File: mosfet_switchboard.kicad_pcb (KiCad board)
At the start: 2 copper layers, 5 parts, among them J1 Conn_01x02_Male, J2 Power Output, J3 Power Input, U1 ZXGD3006E6

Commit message: use USB-C and add analog filtering
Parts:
- removed J1: Conn_01x02_Male, Connector_PinSocket_2.54mm:PinSocket_1x02_P2.54mm_Vertical
- removed J2: Power Output, TerminalBlock_RND:TerminalBlock_RND_205-00287_1x02_P5.08mm_Horizontal
- removed J3: Power Input, TerminalBlock_RND:TerminalBlock_RND_205-00287_1x02_P5.08mm_Horizontal
- removed R1: 100Ω, Resistor_SMD:R_0402_1005Metric
- removed U1: ZXGD3006E6, Package_TO_SOT_SMD:SOT-23-6

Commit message: initial component placement
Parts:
- added C1: 220pF, Capacitor_SMD:C_0603_1608Metric, F.Cu at (146.0, 56.0)
- added C10: 100nF, Capacitor_SMD:C_0603_1608Metric, F.Cu at (138.0, 70.8)
- added C11: 10nF, Capacitor_SMD:C_0603_1608Metric, F.Cu at (145.2, 75.2)
- added C12: 100nF, Capacitor_SMD:C_0603_1608Metric, F.Cu at (137.0, 73.8)
- added C13: 1µF, Capacitor_SMD:C_0603_1608Metric, F.Cu at (147.0, 75.2)
- added C14: 4.7µF, Capacitor_SMD:C_0603_1608Metric, F.Cu at (135.0, 75.2)
- added C15: 4.7µF, Capacitor_SMD:C_0603_1608Metric, F.Cu at (138.8, 73.8)
- added C16: 4.7µF, Capacitor_SMD:C_0603_1608Metric, F.Cu at (145.2, 87.2)
- added C2: 220pF, Capacitor_SMD:C_0603_1608Metric, F.Cu at (146.0, 105.0)
- added C3: 220pF, Capacitor_SMD:C_0603_1608Metric, F.Cu at (146.2, 92.0)
- added C4: 220pF, Capacitor_SMD:C_0603_1608Metric, F.Cu at (145.0, 70.0)
- added C5: 10µF, Capacitor_SMD:C_0603_1608Metric, F.Cu at (141.0, 42.0)
- added C6: 10µF, Capacitor_SMD:C_0603_1608Metric, F.Cu at (132.0, 48.0)
- added C7: 100nF, Capacitor_SMD:C_0603_1608Metric, F.Cu at (133.2, 80.5)
- added C8: 100nF, Capacitor_SMD:C_0603_1608Metric, F.Cu at (133.2, 77.2)
- added C9: 100nF, Capacitor_SMD:C_0603_1608Metric, F.Cu at (147.0, 85.5)
- added D1: GREEN, LED_SMD:LED_0603_1608Metric, F.Cu at (161.2, 96.0)
- added D10: BZX84C3V3-T1, Diode_SMD:D_SOT-23_ANK, F.Cu at (151.0, 114.0)
- added D11: BZX84C3V3-T1, Diode_SMD:D_SOT-23_ANK, F.Cu at (151.0, 48.0)
- added D12: BZX84C3V3-T1, Diode_SMD:D_SOT-23_ANK, F.Cu at (152.0, 95.0)
- added D13: BZX84C3V3-T1, Diode_SMD:D_SOT-23_ANK, F.Cu at (151.0, 66.0)
- added D14: BZX84C3V3-T1, Diode_SMD:D_SOT-23_ANK, F.Cu at (151.0, 44.0)
- added D15: BZX84C3V3-T1, Diode_SMD:D_SOT-23_ANK, F.Cu at (152.0, 105.0)
- added D16: BZX84C3V3-T1, Diode_SMD:D_SOT-23_ANK, F.Cu at (151.0, 62.0)
- added D17: BZX84C3V3-T1, Diode_SMD:D_SOT-23_ANK, F.Cu at (152.0, 86.0)
- added D18: BLUE, LED_SMD:LED_0603_1608Metric, F.Cu at (132.0, 32.8)
- added D2: GREEN, LED_SMD:LED_0603_1608Metric, F.Cu at (161.2, 76.0)
- added D3: GREEN, LED_SMD:LED_0603_1608Metric, F.Cu at (161.0, 56.0)
- added D4: GREEN, LED_SMD:LED_0603_1608Metric, F.Cu at (161.0, 116.0)
- added D5: RED, LED_SMD:LED_0603_1608Metric, F.Cu at (157.0, 116.0)
- added D6: RED, LED_SMD:LED_0603_1608Metric, F.Cu at (157.2, 56.0)
- added D7: RED, LED_SMD:LED_0603_1608Metric, F.Cu at (157.0, 96.0)
- added D8: RED, LED_SMD:LED_0603_1608Metric, F.Cu at (157.2, 76.0)
- added D9: BZX84C3V3-T1, Diode_SMD:D_SOT-23_ANK, F.Cu at (157.0, 130.0)
- added FB1: 100Ohm @ 100MHz, Inductor_SMD:L_0805_2012Metric, F.Cu at (137.2, 40.9)
- added J1: Power Output, TerminalBlock_RND:TerminalBlock_RND_205-00287_1x02_P5.08mm_Horizontal, F.Cu at (177.0, 50.0)
- added J2: Power Output, TerminalBlock_RND:TerminalBlock_RND_205-00287_1x02_P5.08mm_Horizontal, F.Cu at (177.0, 70.0)
- added J3: Power Output, TerminalBlock_RND:TerminalBlock_RND_205-00287_1x02_P5.08mm_Horizontal, F.Cu at (177.0, 90.0)
- added J4: Power Output, TerminalBlock_RND:TerminalBlock_RND_205-00287_1x02_P5.08mm_Horizontal, F.Cu at (177.0, 110.0)
- added J5: Power Input, TerminalBlock_RND:TerminalBlock_RND_205-00287_1x02_P5.08mm_Horizontal, F.Cu at (165.0, 30.0)
- added J6: Power Input, TerminalBlock_RND:TerminalBlock_RND_205-00287_1x02_P5.08mm_Horizontal, F.Cu at (170.1, 133.0)
- added J7: USB_C_Receptacle_USB2.0, Connector_USB:USB_C_Receptacle_Amphenol_12401610E4-2A, B.Cu at (139.2, 29.0)
- added J8: Conn_01x04_Male, Connector_PinHeader_2.54mm:PinHeader_1x04_P2.54mm_Vertical, F.Cu at (153.0, 34.0)
- added J9: Conn_ARM_JTAG_SWD_10, Connector_PinHeader_1.27mm:PinHeader_2x05_P1.27mm_Vertical_SMD, F.Cu at (135.0, 106.0)
- added JP1: SolderJumper_2_Open, Jumper:SolderJumper-2_P1.3mm_Open_RoundedPad1.0x1.5mm, F.Cu at (132.5, 73.5)
- added JP3: SolderJumper_2_Open, Jumper:SolderJumper-2_P1.3mm_Open_RoundedPad1.0x1.5mm, F.Cu at (132.8, 87.2)
- added JP8: SolderJumper_3_Bridged12, Jumper:SolderJumper-3_P1.3mm_Bridged12_RoundedPad1.0x1.5mm_NumberLabels, F.Cu at (147.8, 36.8)
- added L1: 39nH, Inductor_SMD:L_0603_1608Metric, F.Cu at (143.5, 73.8)
- added R1: 12kΩ, Resistor_SMD:R_0603_1608Metric, F.Cu at (161.0, 125.0)
- added R10: 10kΩ, Resistor_SMD:R_0603_1608Metric, F.Cu at (161.2, 100.0)
- added R11: 10kΩ, Resistor_SMD:R_0603_1608Metric, F.Cu at (161.2, 80.0)
- added R12: 10kΩ, Resistor_SMD:R_0603_1608Metric, F.Cu at (161.0, 120.0)
- added R13: 10kΩ, Resistor_SMD:R_0603_1608Metric, F.Cu at (161.0, 60.0)
- added R14: 10kΩ, Resistor_SMD:R_0603_1608Metric, F.Cu at (157.0, 120.0)
- added R15: 10kΩ, Resistor_SMD:R_0603_1608Metric, F.Cu at (157.0, 80.0)
- added R16: 10kΩ, Resistor_SMD:R_0603_1608Metric, F.Cu at (157.0, 100.0)
- added R17: 10kΩ, Resistor_SMD:R_0603_1608Metric, F.Cu at (157.0, 60.0)
- added R18: 4.7kΩ, Resistor_SMD:R_0603_1608Metric, F.Cu at (155.0, 71.0)
- added R19: 4.7kΩ, Resistor_SMD:R_0603_1608Metric, F.Cu at (156.0, 89.0)
- added R2: 1.8kΩ, Resistor_SMD:R_0603_1608Metric, F.Cu at (157.0, 125.0)
- added R20: 4.7kΩ, Resistor_SMD:R_0603_1608Metric, F.Cu at (155.0, 51.0)
- added R21: 4.7kΩ, Resistor_SMD:R_0603_1608Metric, F.Cu at (155.0, 109.0)
- added R22: 4.7kΩ, Resistor_SMD:R_0603_1608Metric, F.Cu at (151.0, 111.0)
- added R23: 4.7kΩ, Resistor_SMD:R_0603_1608Metric, F.Cu at (151.8, 91.0)
- added R24: 4.7kΩ, Resistor_SMD:R_0603_1608Metric, F.Cu at (150.8, 69.0)
- added R25: 4.7kΩ, Resistor_SMD:R_0603_1608Metric, F.Cu at (151.0, 51.0)
- added R26: 4.7kΩ, Resistor_SMD:R_0603_1608Metric, F.Cu at (159.0, 113.0)
- added R27: 4.7kΩ, Resistor_SMD:R_0603_1608Metric, F.Cu at (159.0, 93.0)
- added R28: 4.7kΩ, Resistor_SMD:R_0603_1608Metric, F.Cu at (159.0, 73.0)
- added R29: 4.7kΩ, Resistor_SMD:R_0603_1608Metric, F.Cu at (159.0, 53.0)
- added R3: 5.1kΩ 1%, Resistor_SMD:R_0603_1608Metric, F.Cu at (138.2, 37.0)
- added R30: 8.2kΩ, Resistor_SMD:R_0603_1608Metric, F.Cu at (159.0, 88.8)
- added R31: 8.2kΩ, Resistor_SMD:R_0603_1608Metric, F.Cu at (159.0, 69.0)
- added R32: 8.2kΩ, Resistor_SMD:R_0603_1608Metric, F.Cu at (159.0, 109.0)
- added R33: 8.2kΩ, Resistor_SMD:R_0603_1608Metric, F.Cu at (159.0, 49.0)
- added R34: 1.8kΩ, Resistor_SMD:R_0603_1608Metric, F.Cu at (157.0, 85.0)
- added R35: 1.8kΩ, Resistor_SMD:R_0603_1608Metric, F.Cu at (157.2, 45.0)
- added R36: 1.8kΩ, Resistor_SMD:R_0603_1608Metric, F.Cu at (157.0, 65.0)
- added R37: 1.8kΩ, Resistor_SMD:R_0603_1608Metric, F.Cu at (157.0, 105.0)
- added R38: 10kΩ, Resistor_SMD:R_0603_1608Metric, F.Cu at (133.2, 83.8)
- added R39: 12kΩ, Resistor_SMD:R_0603_1608Metric, F.Cu at (161.2, 45.0)
- added R4: 10kΩ, Resistor_SMD:R_0603_1608Metric, F.Cu at (132.8, 70.5)
- added R40: 12kΩ, Resistor_SMD:R_0603_1608Metric, F.Cu at (161.0, 65.0)
- added R41: 12kΩ, Resistor_SMD:R_0603_1608Metric, F.Cu at (161.0, 105.0)
- added R42: 12kΩ, Resistor_SMD:R_0603_1608Metric, F.Cu at (161.0, 85.0)
- added R43: 10kΩ, Resistor_SMD:R_0603_1608Metric, F.Cu at (132.0, 37.0)
- added R5: 4.7kΩ, Resistor_SMD:R_0603_1608Metric, F.Cu at (146.0, 54.0)
- added R6: 4.7kΩ, Resistor_SMD:R_0603_1608Metric, F.Cu at (146.0, 107.0)
- added R7: 4.7kΩ, Resistor_SMD:R_0603_1608Metric, F.Cu at (145.0, 68.0)
- added R8: 4.7kΩ, Resistor_SMD:R_0603_1608Metric, F.Cu at (146.2, 94.0)
- added R9: 5.1kΩ 1%, Resistor_SMD:R_0603_1608Metric, F.Cu at (146.0, 31.5)
- added U1: BTS7004-1EPP, Package_SO:Infineon_PG-TSDSO-14-22, F.Cu at (165.0, 50.0)
- added U2: BTS7004-1EPP, Package_SO:Infineon_PG-TSDSO-14-22, F.Cu at (165.0, 70.0)
- added U3: BTS7004-1EPP, Package_SO:Infineon_PG-TSDSO-14-22, F.Cu at (165.0, 90.0)
- added U4: BTS7004-1EPP, Package_SO:Infineon_PG-TSDSO-14-22, F.Cu at (165.0, 110.0)
- added U5: AMS1117-3.3, Package_TO_SOT_SMD:SOT-223-3_TabPin2, F.Cu at (138.2, 47.0)
- added U6: STM32F042C4Tx, Package_QFP:LQFP-48_7x7mm_P0.5mm, F.Cu at (140.0, 81.0)
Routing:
- net VDD: track 0.00 -> 105.1 mm

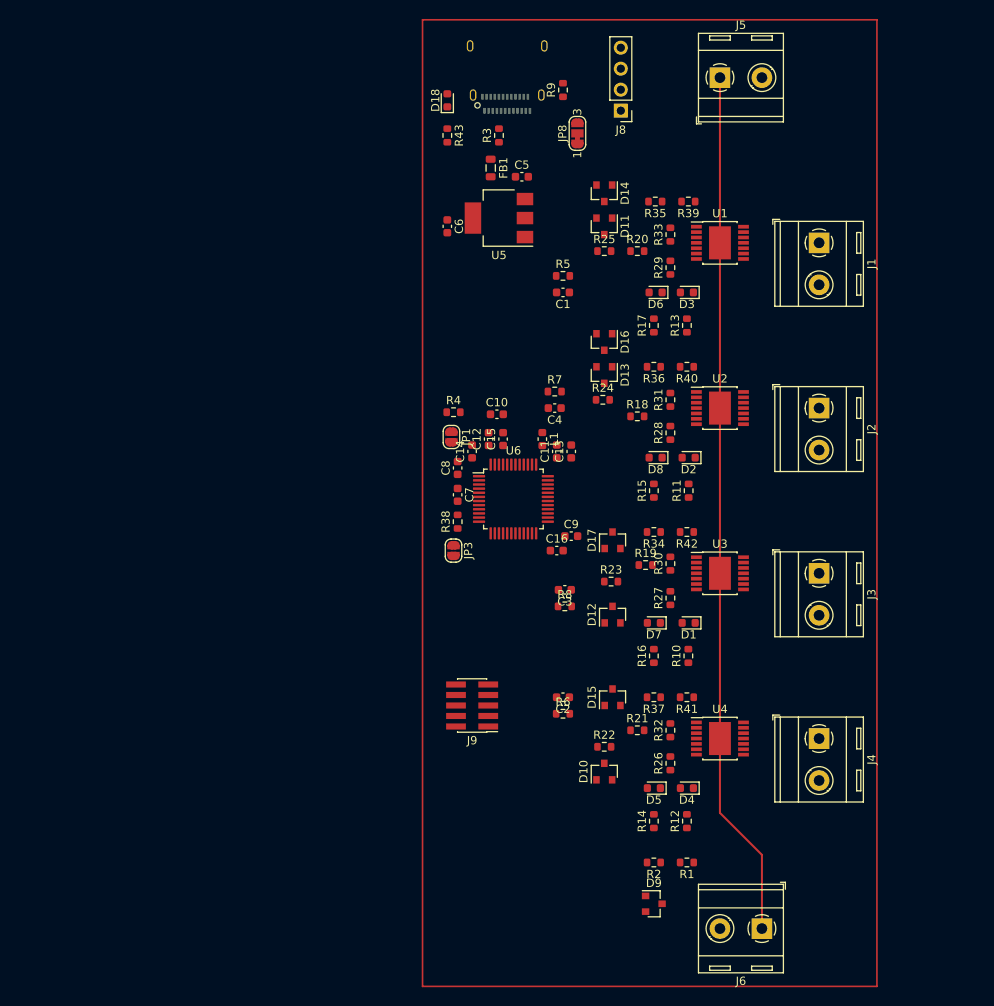
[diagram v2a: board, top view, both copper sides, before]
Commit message: updated footprints, adjustments in placement
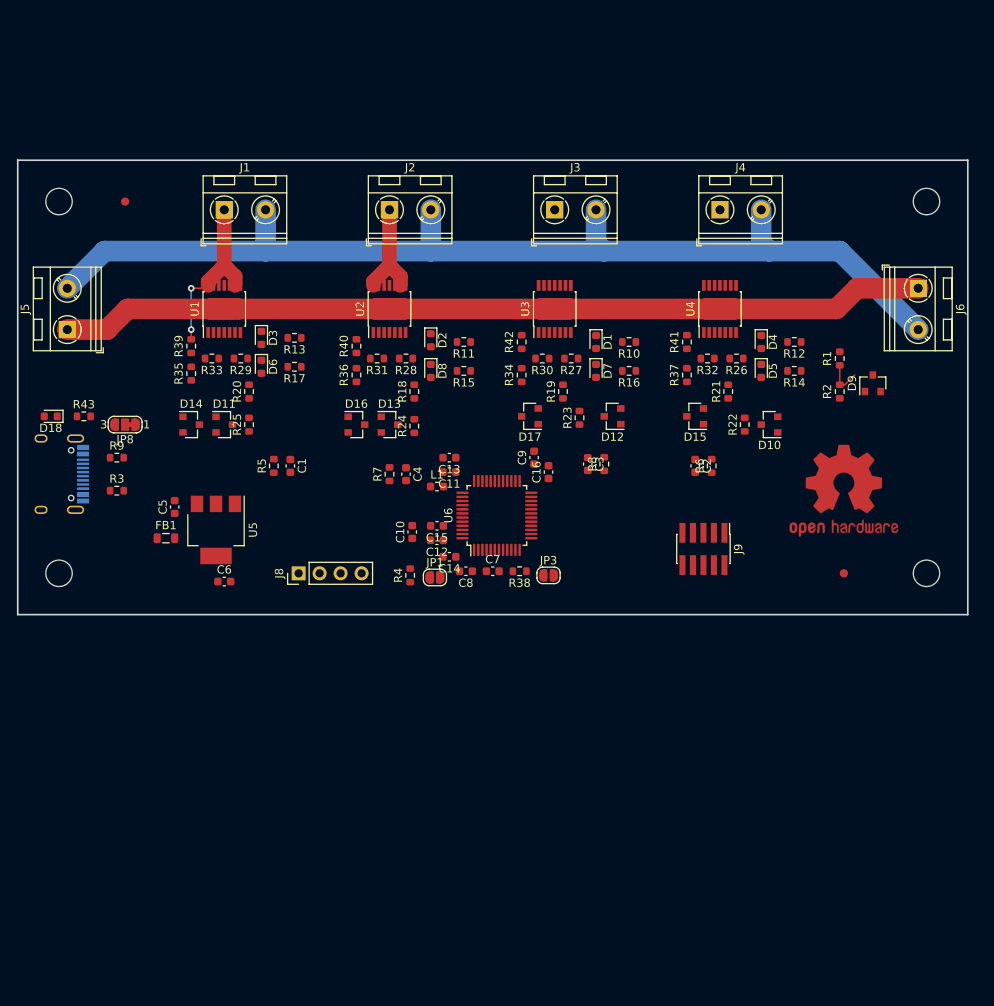
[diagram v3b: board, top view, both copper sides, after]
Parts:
- added REF**: MountingHole_3.2mm_M3, MountingHole:MountingHole_3.2mm_M3, F.Cu at (85.0, 45.0)
- added REF**: OSHW-Logo2_14.6x12mm_Copper, Symbol:OSHW-Logo2_14.6x12mm_Copper, F.Cu at (180.0, 80.0)
- added REF**: MountingHole_3.2mm_M3, MountingHole:MountingHole_3.2mm_M3, F.Cu at (190.0, 90.0)
- added REF**: MountingHole_3.2mm_M3, MountingHole:MountingHole_3.2mm_M3, F.Cu at (85.0, 90.0)
- added REF**: Fiducial_1mm_Mask2mm, Fiducial:Fiducial_1mm_Mask2mm, F.Cu at (93.0, 45.0)
- added REF**: Fiducial_1mm_Mask2mm, Fiducial:Fiducial_1mm_Mask2mm, F.Cu at (180.0, 90.0)
- added REF**: MountingHole_3.2mm_M3, MountingHole:MountingHole_3.2mm_M3, F.Cu at (190.0, 45.0)
- J1, J2, J3, J4, J5, J6: footprint TerminalBlock_RND:TerminalBlock_RND_205-00287_1x02_P5.08mm_Horizontal -> TerminalBlock_RND:TerminalBlock_RND_205-00045_1x02_P5.00mm_Horizontal
- J7: footprint Connector_USB:USB_C_Receptacle_Amphenol_12401610E4-2A -> Connector_USB:USB_C_Receptacle_HRO_TYPE-C-31-M-12
- moved J5 84.7 mm to (86.0, 60.5), turned to 90 degrees
- moved J6 79.8 mm to (189.0, 55.5), turned to -90 degrees
- moved J7 73.9 mm to (83.9, 78.0), turned to 90 degrees
- moved J1 72.1 mm to (105.0, 46.0), turned to 0 degrees
- moved R9 70.0 mm to (92.0, 76.0), turned to 0 degrees
- moved D9 68.3 mm to (183.5, 67.0), turned to 90 degrees
- moved J8 68.2 mm to (114.0, 90.0), turned to 90 degrees
- moved JP8 65.1 mm to (93.0, 72.0), turned to 180 degrees
- moved J4 65.1 mm to (165.0, 46.0), turned to 0 degrees
- moved R1 63.7 mm to (179.5, 64.0), turned to -90 degrees
- moved R3 63.2 mm to (92.0, 80.0), turned to 0 degrees
- moved R39 62.7 mm to (101.0, 62.5), turned to -90 degrees
- moved D18 61.4 mm to (84.0, 71.0), turned to 180 degrees
- moved R2 61.3 mm to (179.5, 68.0), turned to -90 degrees
- moved U1 60.5 mm to (105.0, 58.0), turned to 90 degrees
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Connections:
- net Net-(J1-Pad1) renamed /Power/Power Switch 1/VDD_SWITCHED
- net Net-(J2-Pad1) renamed /Power/Power Switch 2/VDD_SWITCHED
- net Net-(J3-Pad1) renamed /Power/Power Switch 3/VDD_SWITCHED
- net Net-(J4-Pad1) renamed /Power/Power Switch 4/VDD_SWITCHED
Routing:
- net GND: track 0.00 -> 129.6 mm
- net /Power/Power Switch 1/VDD_SWITCHED: track 0.00 -> 21.3 mm, vias 0 -> 2
- net /Power/Power Switch 2/VDD_SWITCHED: track 0.00 -> 13.2 mm
- net INPUT_ADC_U: track 0.00 -> 4.64 mm
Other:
- board outline added: 115 x 55 mm

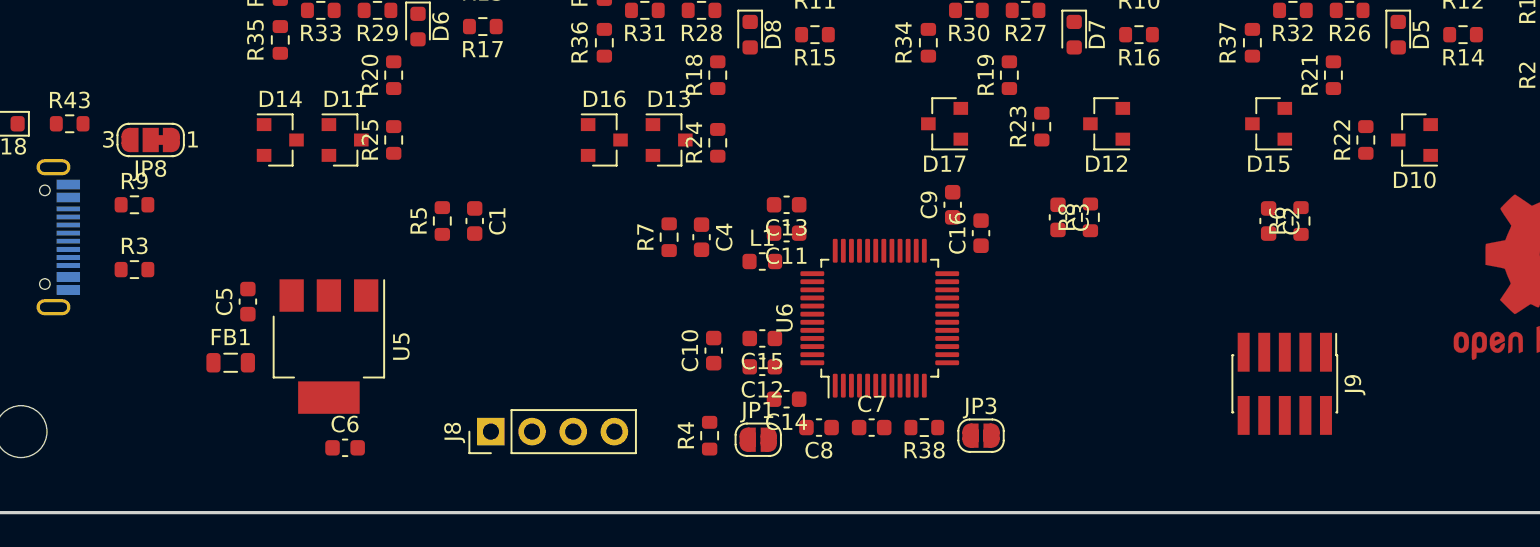
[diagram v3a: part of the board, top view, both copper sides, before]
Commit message: place decoupling capacitors nicer, add USB ESD protection
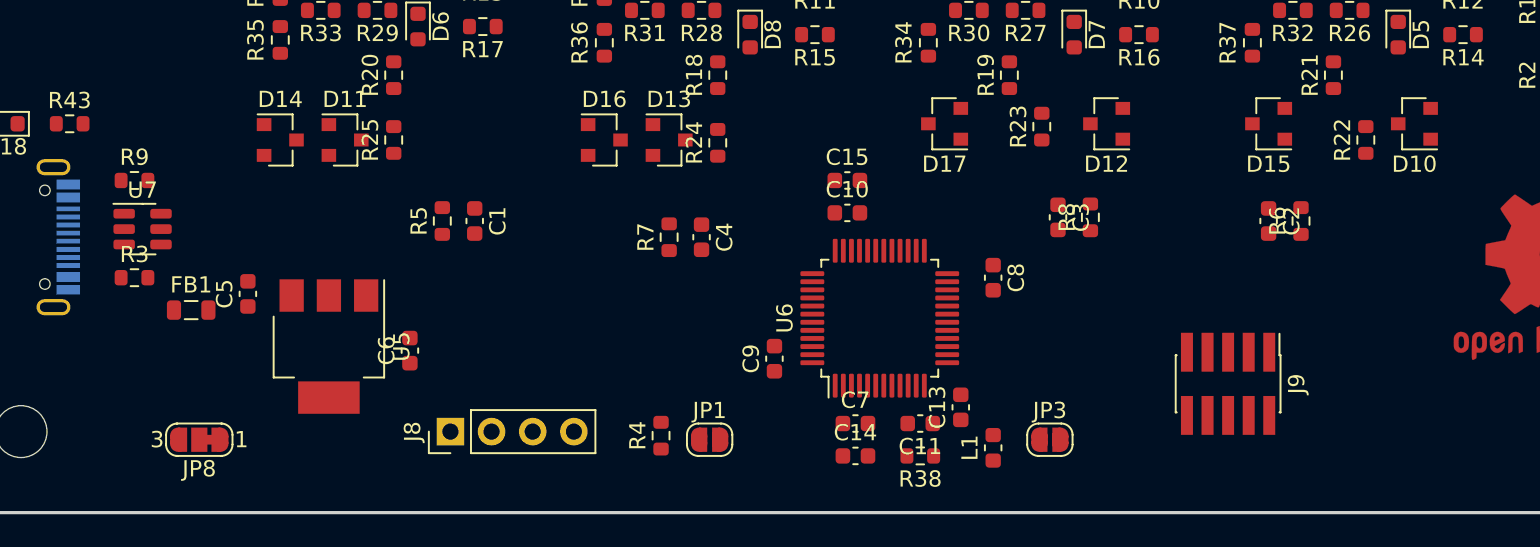
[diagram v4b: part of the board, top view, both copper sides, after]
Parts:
- removed C12: 100nF, Capacitor_SMD:C_0603_1608Metric
- removed C16: 4.7µF, Capacitor_SMD:C_0603_1608Metric
- added U7: USBLC6-2SC6, Package_TO_SOT_SMD:SOT-23-6, F.Cu at (92.5, 77.5)
- moved JP8 18.7 mm to (96.0, 90.5)
- moved L1 18.3 mm to (145.0, 91.0), turned to 90 degrees
- moved C13 16.5 mm to (143.0, 88.5), turned to 90 degrees
- moved C9 14.5 mm to (131.5, 85.5)
- moved C11 14.4 mm to (140.5, 89.5)
- moved C8 14.2 mm to (145.0, 80.5), turned to -90 degrees
- moved C10 11.8 mm to (136.0, 76.5), turned to 0 degrees
- moved C15 11.1 mm to (136.0, 74.5), turned to 0 degrees
- moved C6 7.21 mm to (109.0, 85.0), turned to 90 degrees
- moved C14 5.51 mm to (136.5, 91.5), turned to 0 degrees
- moved JP3 4.26 mm to (148.5, 90.5)
- moved FB1 4.06 mm to (95.5, 82.5)
- moved J9 3.50 mm to (159.5, 87.0)
- moved JP1 3.00 mm to (127.5, 90.5)
- moved R4 3.00 mm to (124.5, 90.2)
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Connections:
- J7 pad A6: /Control/USB_DP -> /Control/USB_CONN_DP
- J7 pad A7: /Control/USB_DM -> /Control/USB_CONN_DM
- J7 pad B6: /Control/USB_DP -> /Control/USB_CONN_DP
- J7 pad B7: /Control/USB_DM -> /Control/USB_CONN_DM
- U6 pad 36: +3.3VA -> +3V3
- U6 pad 9: +3V3 -> +3.3VA
